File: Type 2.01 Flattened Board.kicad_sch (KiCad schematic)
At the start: 7 parts

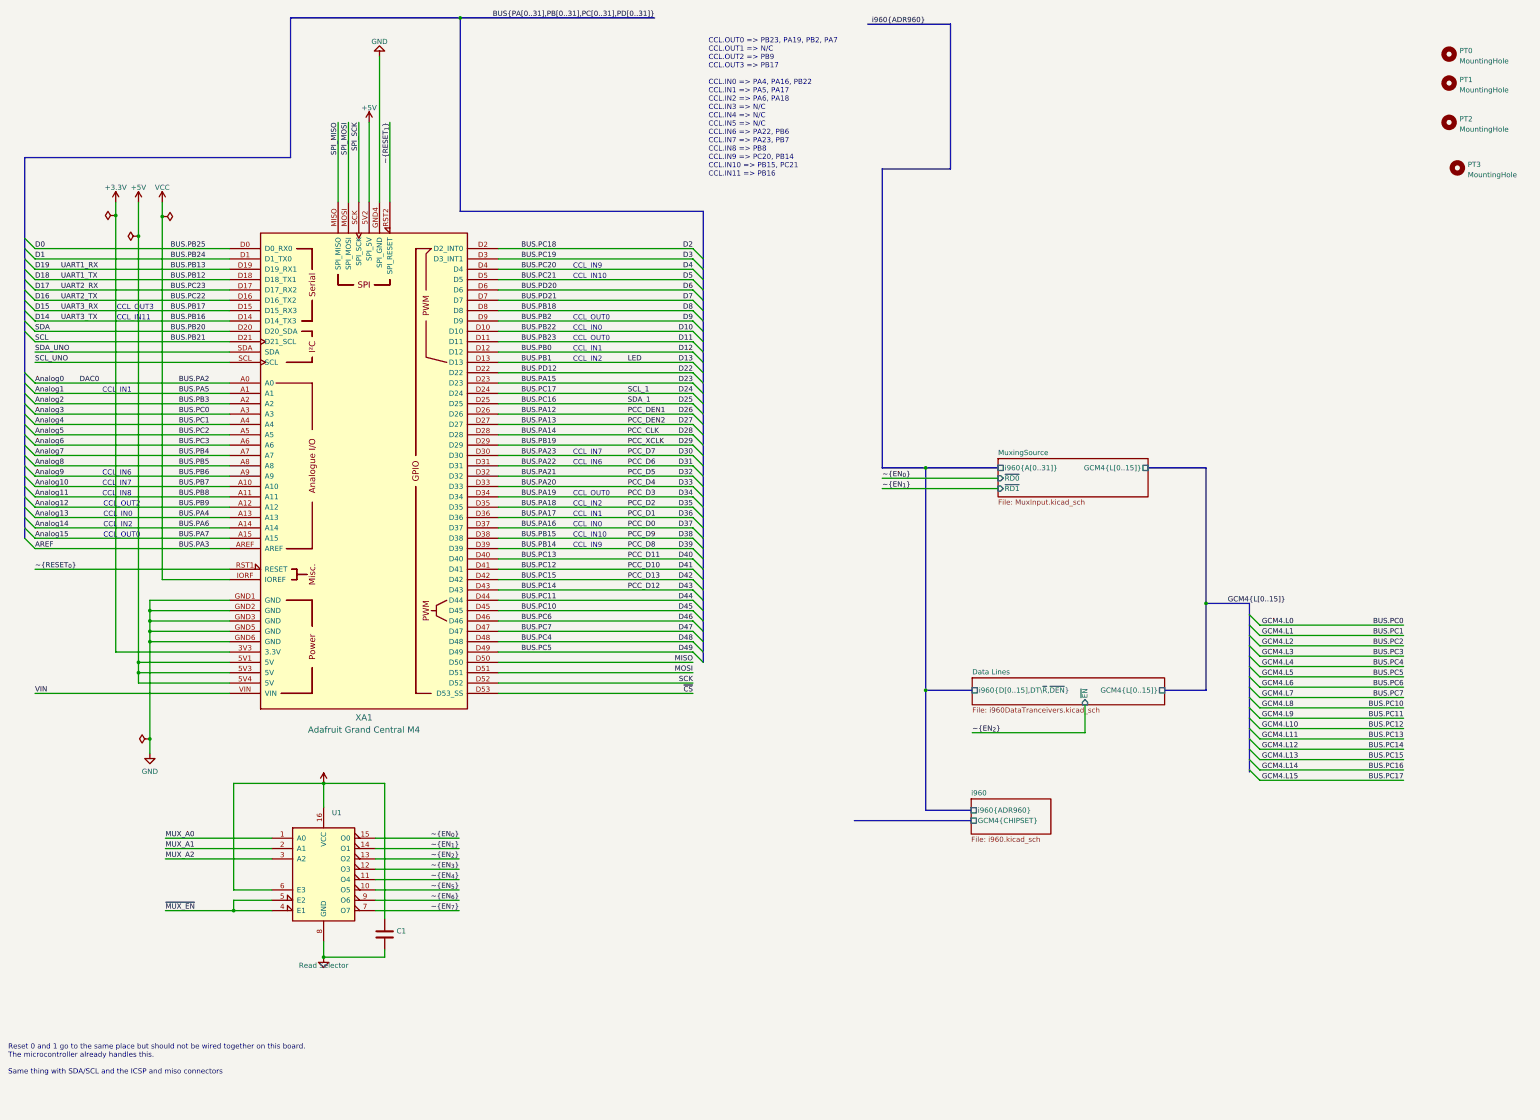
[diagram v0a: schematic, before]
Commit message: Move extraneous signals to register 4
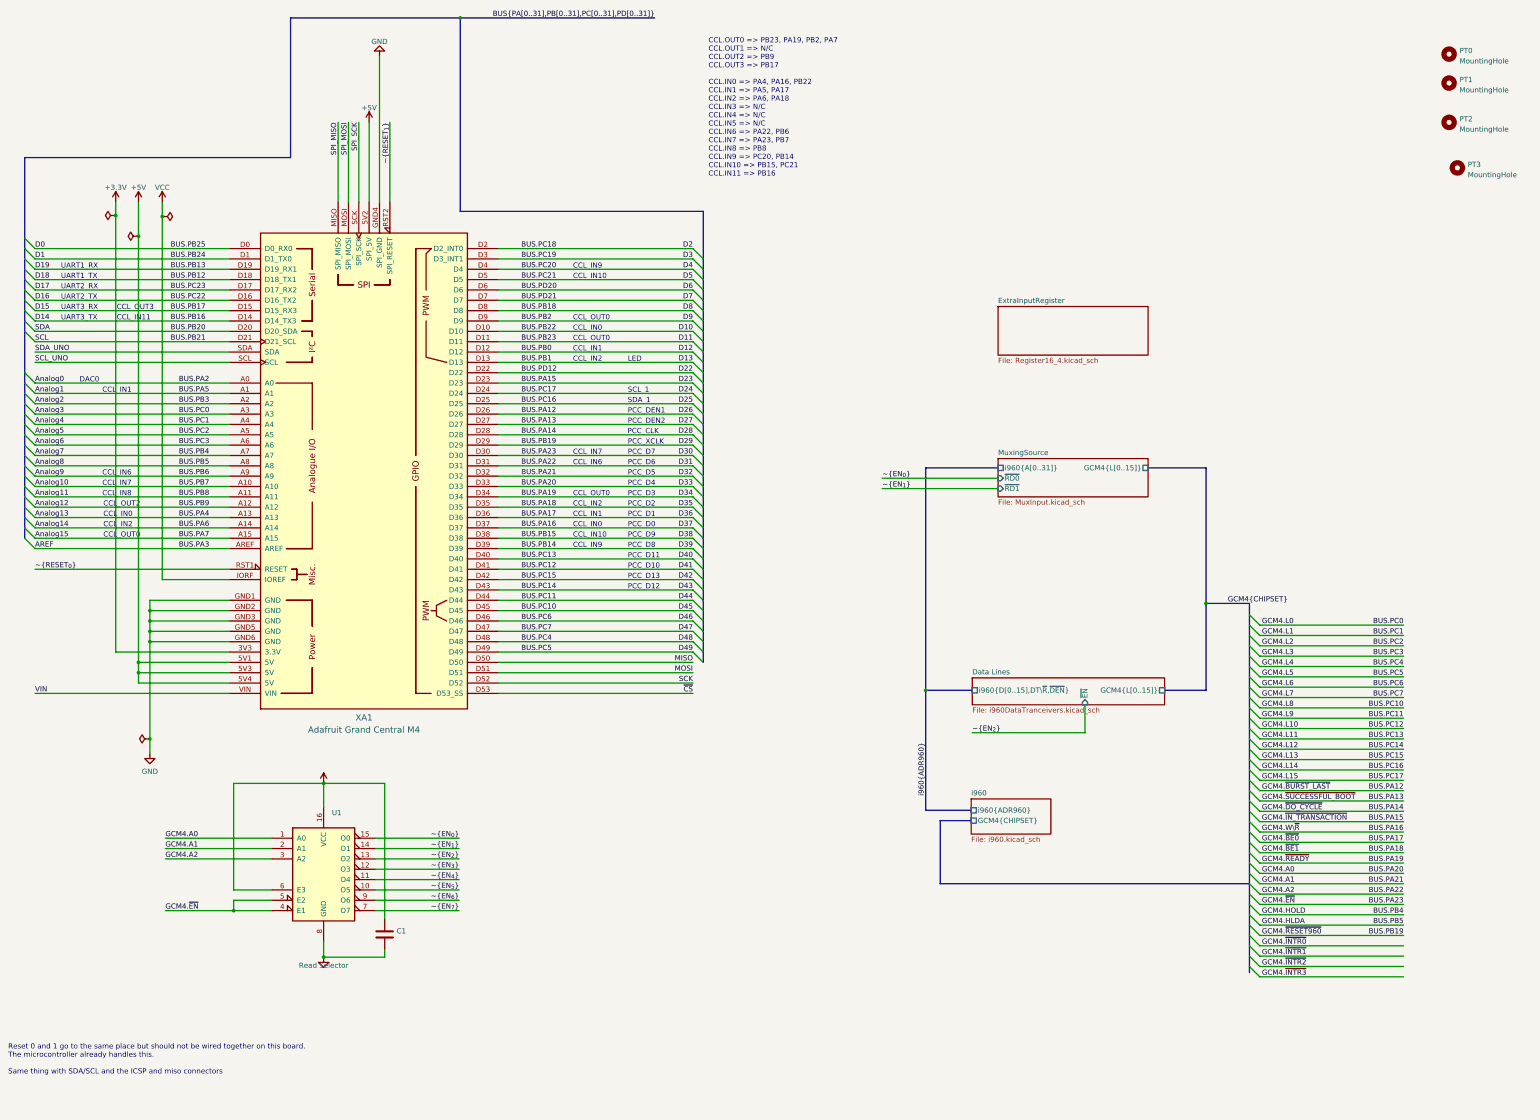
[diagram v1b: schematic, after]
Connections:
- net MUX_A0 is gone; now on net BUS.PA20: U1.1 (A0)
- net MUX_A1 is gone; now on net BUS.PA21: U1.2 (A1)
- net MUX_A2 is gone; now on net BUS.PA22: U1.3 (A2)
- net ~{MUX_EN} is gone; now on net BUS.PA23: U1.4 (E1), U1.5 (E2)
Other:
- added sheet ExtraInputRegister (Register16_4.kicad_sch)
- note added: "DAC0"
- note added: "LED"
- note added: "PCC_CLK"
- note added: "PCC_D0"
- note added: "PCC_D1"
- note added: "PCC_D10"
- note added: "PCC_D11"
- note added: "PCC_D12"
- note added: "PCC_D13"
- note added: "PCC_D2"
- note added: "PCC_D3"
- note added: "PCC_D4"
- note added: "PCC_D5"
- note added: "PCC_D6"
- note added: "PCC_D7"
- note added: "PCC_D8"
- note added: "PCC_D9"
- note added: "PCC_DEN1"
- note added: "PCC_DEN2"
- note added: "PCC_XCLK"
- note added: "SCL_1"
- note added: "SDA_1"
- note added: "UART1_RX"
- note added: "UART1_TX"
- note added: "UART2_RX"
- note added: "UART2_TX"
- note added: "UART3_RX"
- note added: "UART3_TX"

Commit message: More pinout related actions
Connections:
- net BUS.PA20: no longer U1.1 (A0)
- net BUS.PA21: now also U1.1 (A0); no longer U1.2 (A1)
- net BUS.PA22: now also U1.2 (A1); no longer U1.3 (A2)
- new net GCM4.A2: U1.3 (A2)
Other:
- sheet ExtraInputRegister ports: added GCM4{L[0..15]}, i960{ADR960}, ~{EN}; removed none
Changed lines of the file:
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@@
   (junction (at 54.102 162.052) (diameter 0) (color 0 0 0 0)
   )
+  (junction (at 244.602 127) (diameter 0) (color 0 0 0 0)
+  )
   (junction (at 51.308 70.104) (diameter 0) (color 0 0 0 0)
   )
+  (junction (at 313.436 127) (diameter 0) (color 0 0 0 0)
+  )
   (junction (at 54.102 193.548) (diameter 0) (color 0 0 0 0)
   )
@@
     (stroke (width 0) (type default) (color 0 0 0 0))
   )
+  (bus (pts (xy 299.212 92.456) (xy 313.436 92.456))
+    (stroke (width 0) (type default) (color 0 0 0 0))
+  )
   (bus (pts (xy 23.368 108.712) (xy 23.368 106.172))
     (stroke (width 0) (type default) (color 0 0 0 0))
@@
     (stroke (width 0) (type default) (color 0 0 0 0))
   )
+  (bus (pts (xy 244.602 92.456) (xy 244.602 127))
+    (stroke (width 0) (type default) (color 0 0 0 0))
+  )
   (wire (pts (xy 139.7 78.232) (xy 187.452 78.232))
     (stroke (width 0) (type default) (color 0 0 0 0))
@@
     (stroke (width 0) (type default) (color 0 0 0 0))
   )
+  (bus (pts (xy 313.436 92.456) (xy 313.436 127))
+    (stroke (width 0) (type default) (color 0 0 0 0))
+  )
   (wire (pts (xy 326.644 198.628) (xy 361.95 198.628))
     (stroke (width 0) (type default) (color 0 0 0 0))
@@
     (stroke (width 0) (type default) (color 0 0 0 0))
   )
+  (wire (pts (xy 233.934 96.774) (xy 262.382 96.774))
+    (stroke (width 0) (type default) (color 0 0 0 0))
+  )
   (bus (pts (xy 299.212 127) (xy 313.436 127))
     (stroke (width 0) (type default) (color 0 0 0 0))
@@
   )
   (bus (pts (xy 23.368 144.272) (xy 23.368 141.732))
+    (stroke (width 0) (type default) (color 0 0 0 0))
+  )
+  (bus (pts (xy 262.382 92.456) (xy 244.602 92.456))
     (stroke (width 0) (type default) (color 0 0 0 0))
   )
@@
     (effects (font (size 1.27 1.27)) (justify left bottom))
   )
-  (label "GCM4.~{INTR2}" (at 327.152 249.428 0)
+  (label "GCM4.~{INTR2}" (at 327.152 221.488 0)
     (effects (font (size 1.27 1.27)) (justify left bottom))
   )
@@
     (effects (font (size 1.27 1.27)) (justify left bottom))
   )
-  (label "GCM4.~{INTR0}" (at 327.152 244.348 0)
+  (label "~{EN_{3}}" (at 233.934 96.774 0)
+    (effects (font (size 1.27 1.27)) (justify left bottom))
+  )
+  (label "GCM4.~{INTR0}" (at 327.152 216.408 0)
     (effects (font (size 1.27 1.27)) (justify left bottom))
   )
@@
     (effects (font (size 1.27 1.27)) (justify left bottom))
   )
-  (label "GCM4.A0" (at 327.152 226.568 0)
+  (label "GCM4.A0" (at 327.152 229.108 0)
     (effects (font (size 1.27 1.27)) (justify left bottom))
   )
@@
     (effects (font (size 1.27 1.27)) (justify right bottom))
   )
-  (label "GCM4.~{BE1}" (at 327.152 221.488 0)
-    (effects (font (size 1.27 1.27)) (justify left bottom))
-  )
   (label "D18" (at 25.908 80.772 0)
     (effects (font (size 1.27 1.27)) (justify left bottom))
   )
-  (label "GCM4.A1" (at 327.152 229.108 0)
+  (label "GCM4.A1" (at 327.152 231.648 0)
     (effects (font (size 1.27 1.27)) (justify left bottom))
   )
@@
     (effects (font (size 1.27 1.27)) (justify left bottom))
   )
-  (label "GCM4.~{INTR1}" (at 327.152 246.888 0)
+  (label "GCM4.~{INTR1}" (at 327.152 218.948 0)
     (effects (font (size 1.27 1.27)) (justify left bottom))
   )
@@
     (effects (font (size 1.27 1.27)) (justify left bottom))
   )
-  (label "GCM4.A2" (at 327.152 231.648 0)
-    (effects (font (size 1.27 1.27)) (justify left bottom))
-  )
   (label "GCM4.L4" (at 327.152 175.768 0)
     (effects (font (size 1.27 1.27)) (justify left bottom))
@@
     (effects (font (size 1.27 1.27)) (justify left bottom))
   )
-  (label "GCM4.~{INTR3}" (at 327.152 251.968 0)
+  (label "GCM4.~{INTR3}" (at 327.152 224.028 0)
     (effects (font (size 1.27 1.27)) (justify left bottom))
   )
@@
     (effects (font (size 1.27 1.27)) (justify left bottom))
   )
-  (label "GCM4.W\\~{R}" (at 327.152 216.408 0)
-    (effects (font (size 1.27 1.27)) (justify left bottom))
-  )
   (label "BUS.PD21" (at 145.288 85.852 0)
     (effects (font (size 1.27 1.27)) (justify left bottom))
@@
     (effects (font (size 1.27 1.27)) (justify right bottom))
   )
-  (label "GCM4.~{READY}" (at 327.152 224.028 0)
+  (label "GCM4.~{READY}" (at 327.152 226.568 0)
     (effects (font (size 1.27 1.27)) (justify left bottom))
   )
@@
   (label "~{EN_{3}}" (at 130.048 225.552 180)
     (effects (font (size 1.27 1.27)) (justify right bottom))
-  )
-  (label "GCM4.~{BE0}" (at 327.152 218.948 0)
-    (effects (font (size 1.27 1.27)) (justify left bottom))
   )
   (label "BUS.PA18" (at 145.288 136.652 0)
@@
       (effects (font (size 1.27 1.27)) (justify left top))
     )
-  )
+    (pin "i960{ADR960}" passive (at 262.382 92.456 180)
+      (effects (font (size 1.27 1.27)) (justify left))
+    )
+    (pin "GCM4{L[0..15]}" passive (at 299.212 92.456 0)
+      (effects (font (size 1.27 1.27)) (justify right))
+    )
+    (pin "~{EN}" input (at 262.382 96.774 180)
+      (effects (font (size 1.27 1.27)) (justify left))
+    )
+  )
